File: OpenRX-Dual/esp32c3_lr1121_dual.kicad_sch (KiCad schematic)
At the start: 39 parts, among them T1 0900PC16J0042001E, U1 ESP32-C3FH4, U2 TLV75533PDQNR, U4 LR1121IMLTRT, U5 OW2EL89CENUXFMYLC-32M, X1 CJ17-400001010B20

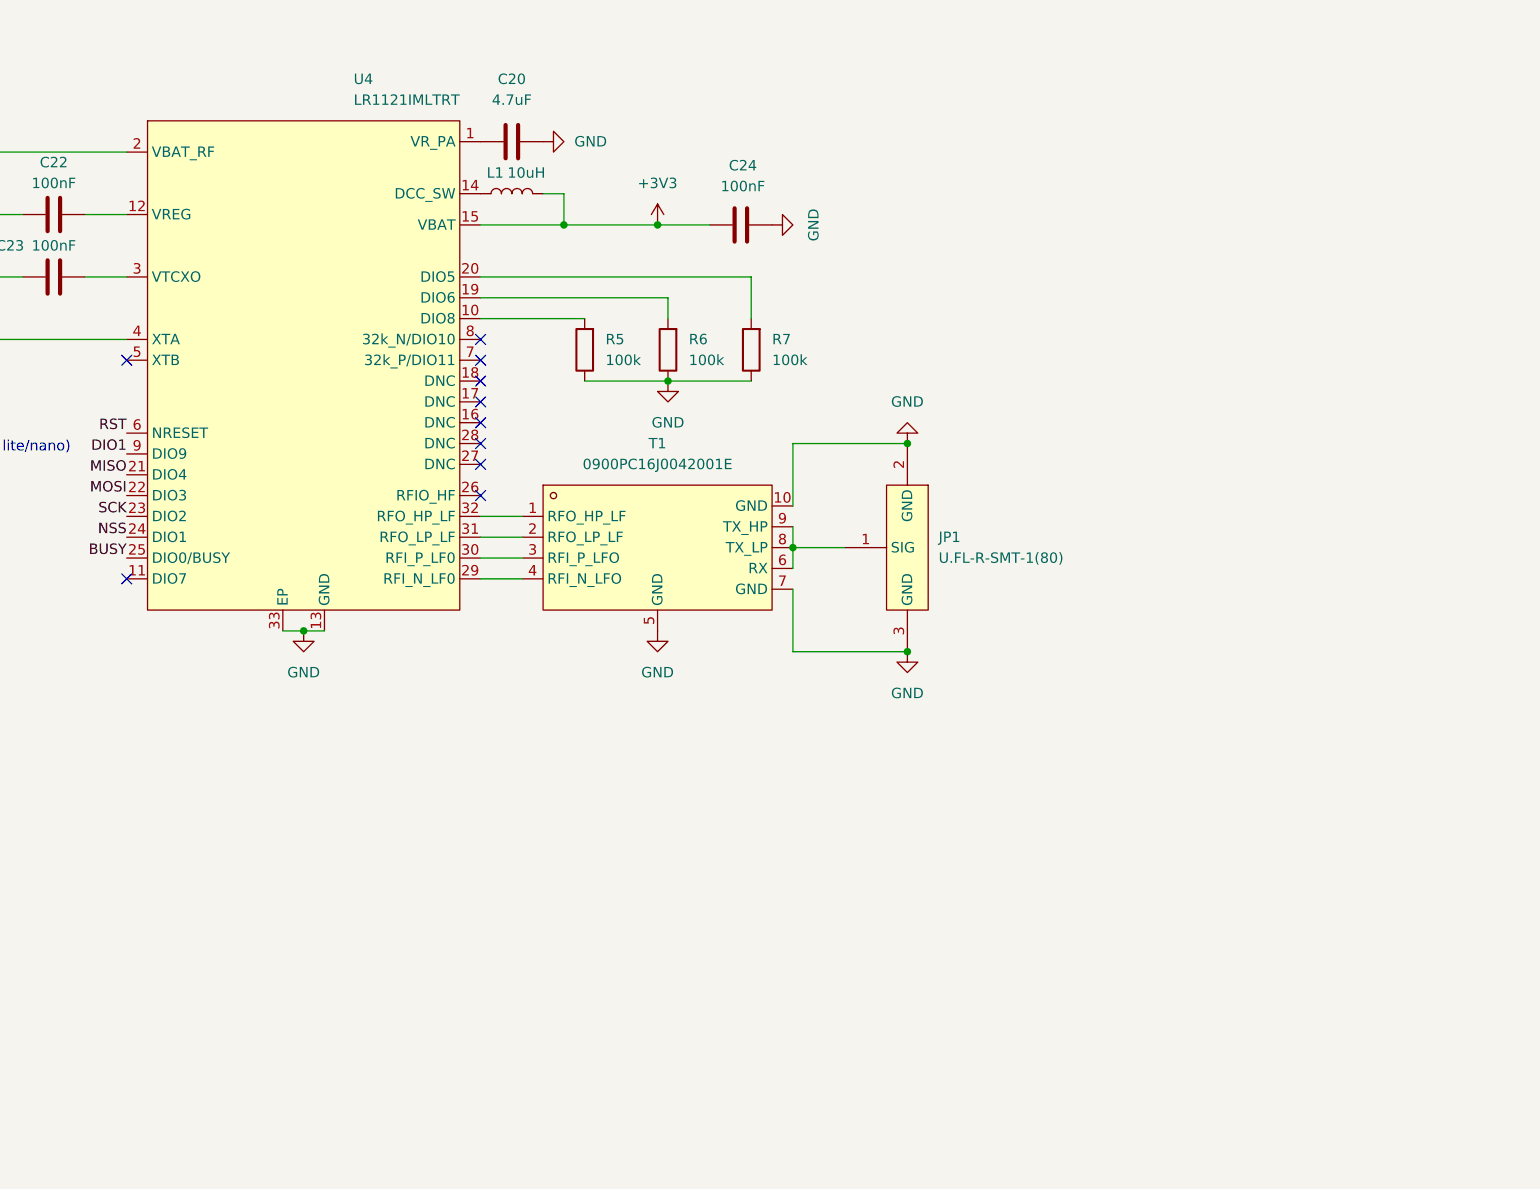
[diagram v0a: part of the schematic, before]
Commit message: OpenRX-Dual: complete schematic, 0 ERC errors, all LCSC fields
Dual-band switchable receiver based on 900 schematic plus:
- RFX2401C (C19213) on 2.4GHz path via DEA LPF
- LR1121 RFSW DIO5/DIO6 drive RFX2401C RXEN/TXEN
- Second UFL for 2.4GHz antenna
- 1uF + 220pF VDD decoupling for RFX2401C
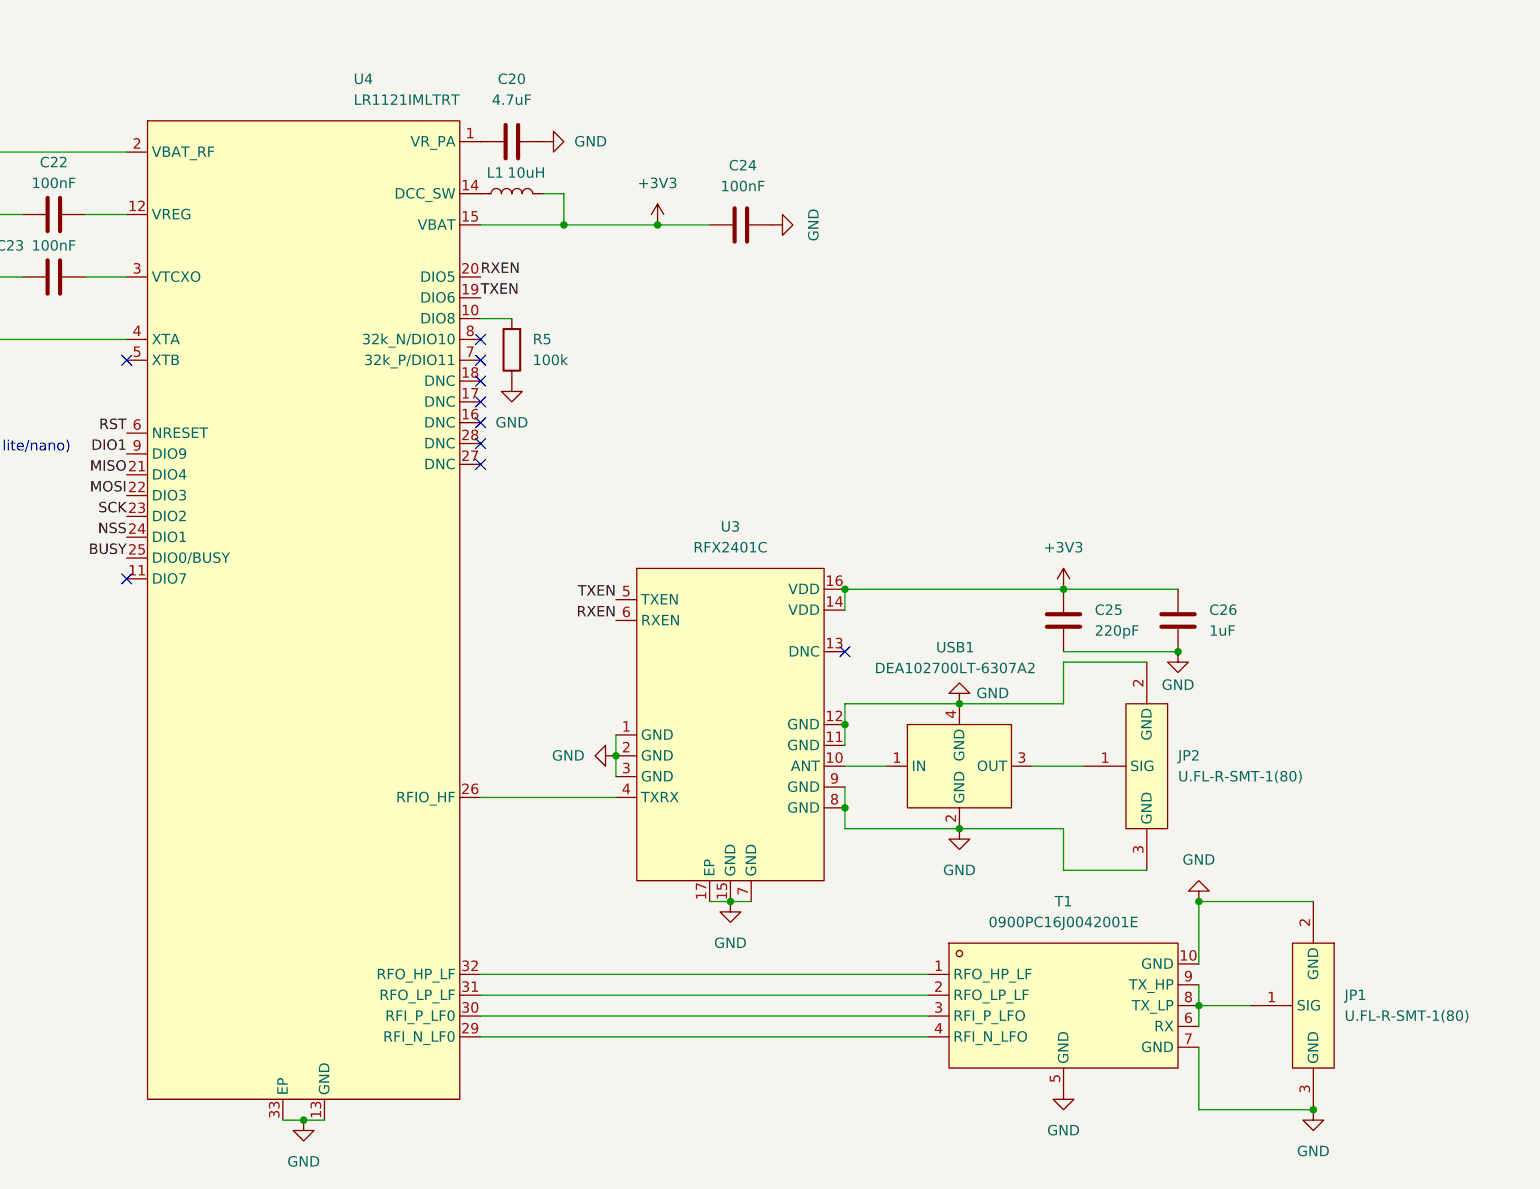
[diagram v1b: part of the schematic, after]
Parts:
- removed R6, R7: 100k, Resistor_SMD:R_0201_0603Metric, symbol Device:R
- added C25: 220pF, Capacitor_SMD:C_0201_0603Metric, symbol Device:C
- added C26: 1uF, Capacitor_SMD:C_0201_0603Metric, symbol Device:C
- added JP2: U.FL-R-SMT-1(80), OpenRX-Shared:RF-SMD_FRF05002-JSS103M, symbol OpenRX-Shared:U.FL-R-SMT-1(80)
- added U3: RFX2401C, OpenRX-Shared:QFN-16_L3.0-W3.0-P0.50-BL-EP1.7, symbol OpenRX-Shared:RFX2401C
- added USB1: DEA102700LT-6307A2, OpenRX-Shared:FILTER-SMD_4P-L1.0-W0.5-L_DEA102700LT-XXX, symbol OpenRX-Shared:DEA102700LT-6307A2
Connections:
- net +3V3: now also C25.1, C26.1, U3.14 (VDD), U3.16 (VDD)
- net GND: now also C25.2, C26.2, JP2.2 (GND), JP2.3 (GND), U3.1 (GND), U3.11 (GND), U3.12 (GND), U3.15 (GND), U3.17 (EP), U3.2 (GND), U3.3 (GND), U3.7 (GND), U3.8 (GND), U3.9 (GND), USB1.2 (GND), USB1.4 (GND)
- net TXEN: now reaches U4.19 (DIO6)
- net TXEN: now also U3.5 (TXEN)
- net RXEN: now reaches U4.20 (DIO5)
- net RXEN: now also U3.6 (RXEN)
- net at U4.26 (RFIO_HF): now also U3.4 (TXRX)
- new net: JP2.1 (SIG), USB1.3 (OUT)
- new net: U3.10 (ANT), USB1.1 (IN)
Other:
- moved on the sheet: JP1, R5, T1, U4

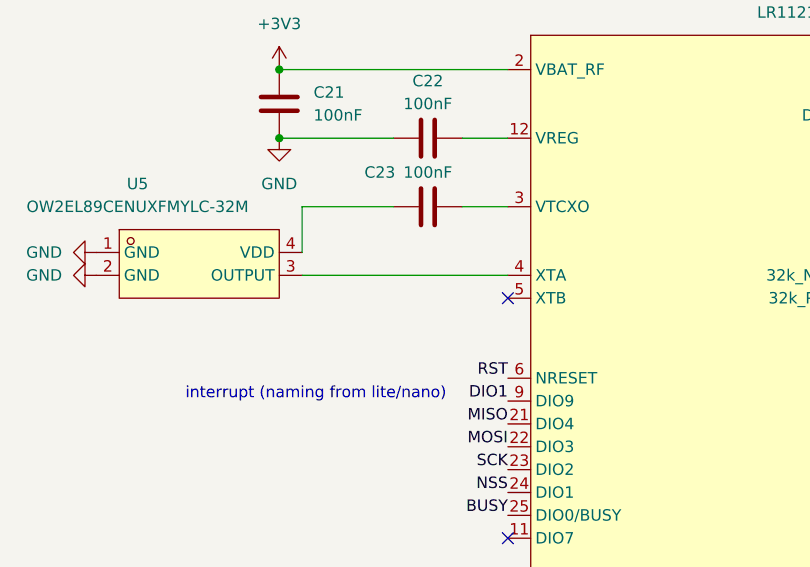
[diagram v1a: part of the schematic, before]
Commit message: Add LCSC to 220R resistor (C25092) in Dual TCXO path
220R series + 10pF DC-cut between TCXO output and LR1121 XTA
per Semtech user manual recommendation.
900 still needs this added in KiCad GUI.
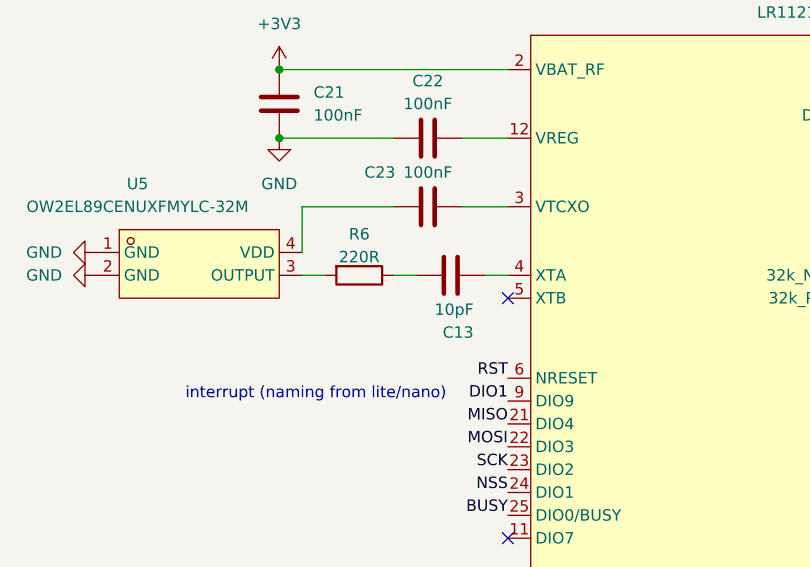
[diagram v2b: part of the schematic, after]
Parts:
- added C13: 10pF, Capacitor_SMD:C_0201_0603Metric, symbol Device:C
- added R6: 220R, Resistor_SMD:R_0201_0603Metric, symbol Device:R
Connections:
- net at U4.4 (XTA): now also C13.2; no longer U5.3 (OUTPUT)
- new net: C13.1, R6.1
- new net: R6.2, U5.3 (OUTPUT)
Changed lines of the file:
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@@
 	(wire
 		(pts
-			(xy 397.51 153.67) (xy 411.48 153.67)
+			(xy 254 59.69) (xy 256.54 59.69)
 		)
 		(stroke
@@
 	(wire
 		(pts
-			(xy 397.51 138.43) (xy 397.51 140.97)
+			(xy 397.51 153.67) (xy 411.48 153.67)
 		)
 		(stroke
@@
 	(wire
 		(pts
-			(xy 309.88 57.15) (xy 313.69 57.15)
+			(xy 397.51 138.43) (xy 397.51 140.97)
 		)
 		(stroke
@@
 	(wire
 		(pts
-			(xy 195.58 121.92) (xy 196.85 121.92)
+			(xy 309.88 57.15) (xy 313.69 57.15)
 		)
 		(stroke
@@
 	(wire
 		(pts
-			(xy 340.36 128.27) (xy 342.9 128.27)
+			(xy 195.58 121.92) (xy 196.85 121.92)
 		)
 		(stroke
@@
 	(wire
 		(pts
-			(xy 243.84 59.69) (xy 266.7 59.69)
+			(xy 340.36 128.27) (xy 342.9 128.27)
 		)
 		(stroke
@@
 	(wire
 		(pts
+			(xy 243.84 59.69) (xy 246.38 59.69)
+		)
+		(stroke
+			(width 0)
+			(type default)
+		)
+	)
+	(wire
+		(pts
 			(xy 381 119.38) (xy 381 124.46)
 		)
@@
 	(wire
 		(pts
+			(xy 264.16 59.69) (xy 266.7 59.69)
+		)
+		(stroke
+			(width 0)
+			(type default)
+		)
+	)
+	(wire
+		(pts
 			(xy 180.34 121.92) (xy 194.31 121.92)
 		)
@@
 		(property "LCSC" "C19213"
 			(at 0 0 0)
+			(hide yes)
 			(show_name no)
 			(do_not_autoplace no)
-			(hide yes)
 			(effects
 				(font
@@
 		(property "LCSC" "C574024"
 			(at 0 0 0)
+			(hide yes)
 			(show_name no)
 			(do_not_autoplace no)
-			(hide yes)
 			(effects
 				(font
@@
 	)
 	(symbol
+		(lib_id "Device:C")
+		(at 260.35 59.69 90)
+		(unit 1)
+		(body_style 1)
+		(exclude_from_sim no)
+		(in_bom yes)
+		(on_board yes)
+		(in_pos_files yes)
+		(dnp no)
+		(property "Reference" "C13"
+			(at 262.89 66.04 90)
+			(show_name no)
+			(do_not_autoplace no)
+			(effects
+				(font
+					(size 1.27 1.27)
+				)
+				(justify left)
+			)
+		)
+		(property "Value" "10pF"
+			(at 262.89 63.5 90)
+			(show_name no)
+			(do_not_autoplace no)
+			(effects
+				(font
+					(size 1.27 1.27)
+				)
+				(justify left)
+			)
+		)
+		(property "Footprint" "Capacitor_SMD:C_0201_0603Metric"
+			(at 264.16 58.7248 0)
+			(hide yes)
+			(show_name no)
+			(do_not_autoplace no)
+			(effects
+				(font
+					(size 1.27 1.27)
+				)
+			)
+		)
+		(property "Datasheet" ""
+			(at 260.35 59.69 0)
+			(hide yes)
+			(show_name no)
+			(do_not_autoplace no)
+			(effects
+				(font
+					(size 1.27 1.27)
+				)
+			)
+		)
+		(property "Description" "Unpolarized capacitor"
+			(at 260.35 59.69 0)
+			(hide yes)
+			(show_name no)
+			(do_not_autoplace no)
+			(effects
+				(font
+					(size 1.27 1.27)
+				)
+			)
+		)
+		(property "LCSC" "C14854"
+			(at 214.63 133.35 0)
+			(hide yes)
+			(show_name no)
+			(do_not_autoplace no)
+			(effects
+				(font
+					(size 1.27 1.27)
+				)
+			)
+		)
+		(pin "1"
+		)
+		(pin "2"
+		)
+		(instances
+			(project "OpenRX-Dual"
+				(path "/b1c2d3e4-f5a6-7890-bcde-f12345678901/f1e2d3c4-b5a6-7890-1234-567890fedcba"
+					(reference "C13")
+					(unit 1)
+				)
+			)
+		)
+	)
+	(symbol
 		(lib_id "power:GND")
 		(at 195.58 121.92 0)
@@
 		(property "LCSC" "C19213"
 			(at 0 0 0)
+			(hide yes)
 			(show_name no)
 			(do_not_autoplace no)
-			(hide yes)
 			(effects
 				(font
@@
 					(unit 1)
 				)
+			)
+		)
+	)
+	(symbol
+		(lib_id "Device:R")
+		(at 250.19 59.69 270)
+		(unit 1)
+		(body_style 1)
+		(exclude_from_sim no)
+		(in_bom yes)
+		(on_board yes)
+		(in_pos_files yes)
+		(dnp no)
+		(property "Reference" "R6"
+			(at 250.19 55.118 90)
+			(show_name no)
+			(do_not_autoplace no)
+			(effects
+				(font
+					(size 1.27 1.27)
+				)
+			)
+		)
+		(property "Value" "220R"
+			(at 250.19 57.658 90)
+			(show_name no)
+			(do_not_autoplace no)
+			(effects
+				(font
+					(size 1.27 1.27)
+				)
+			)
+		)
+		(property "Footprint" "Resistor_SMD:R_0201_0603Metric"
+			(at 250.19 57.912 90)
+			(hide yes)
+			(show_name no)
+			(do_not_autoplace no)
+			(effects
+				(font
+					(size 1.27 1.27)
+				)
+			)
+		)
+		(property "Datasheet" ""
+			(at 250.19 59.69 0)
+			(hide yes)
+			(show_name no)
+			(do_not_autoplace no)
+			(effects
+				(font
+					(size 1.27 1.27)
+				)
+			)
+		)
+		(property "Description" "Resistor"
+			(at 250.19 59.69 0)
+			(hide yes)
+			(show_name no)
+			(do_not_autoplace no)
+			(effects
+				(font
+					(size 1.27 1.27)
+				)
+			)
+		)
+		(property "LCSC" "C25741"
+			(at 189.23 382.27 0)
+			(hide yes)
+			(show_name no)
+			(do_not_autoplace no)
+			(effects
+				(font
+					(size 1.27 1.27)
+				)
+			)
+		)
+		(property "LCSC" "C25092"
+			(at 0 0 0)
+			(show_name no)
+			(do_not_autoplace no)
+			(hide yes)
+			(effects
+				(font
+					(size 1.27 1.27)
+				)
+			)
+		)
+		(pin "2"
+		)
+		(pin "1"
+		)
+		(instances
+			(project "OpenRX-Dual"
+				(path "/b1c2d3e4-f5a6-7890-bcde-f12345678901/f1e2d3c4-b5a6-7890-1234-567890fedcba"
+					(reference "R6")
+					(unit 1)
+				)
